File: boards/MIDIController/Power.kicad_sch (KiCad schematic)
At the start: 3 parts

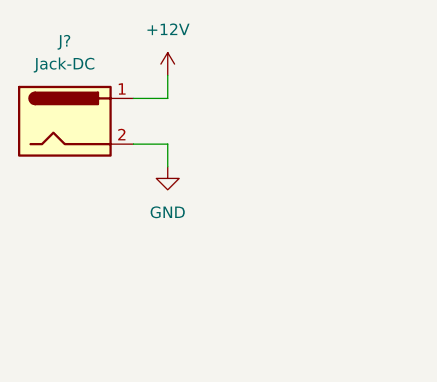
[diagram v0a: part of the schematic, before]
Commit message: Renamed PCBs and updated to KiCAD 7.0
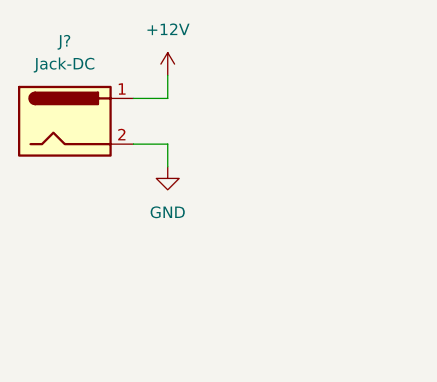
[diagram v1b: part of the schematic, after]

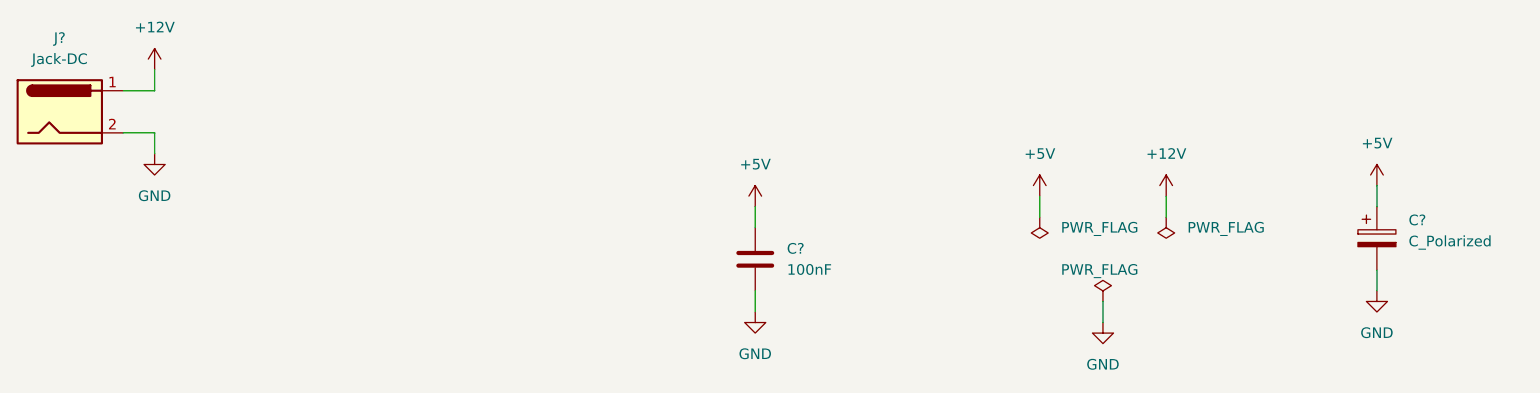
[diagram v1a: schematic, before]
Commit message: Cleanup of PCB sizes and mounthole positions. Moved MIDI connectors to separate board.
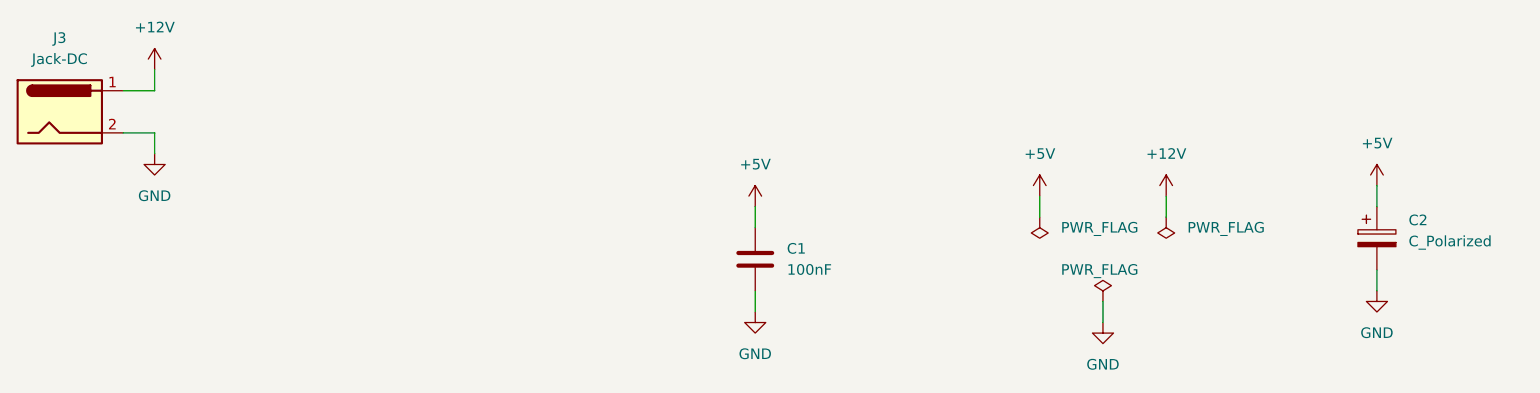
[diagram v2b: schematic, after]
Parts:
- gave numbers to parts that had none: 3

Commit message: Added Optocoupler and RS232 converter to UART board lines.
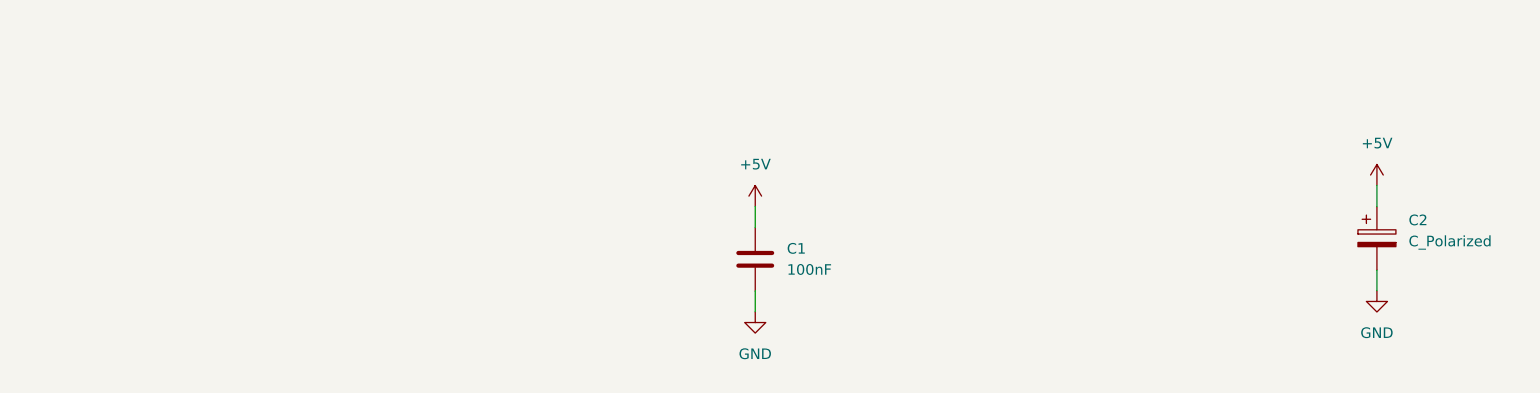
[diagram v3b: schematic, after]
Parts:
- removed J3: Jack-DC, symbol Connector:Jack-DC
